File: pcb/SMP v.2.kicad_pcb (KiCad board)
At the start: 2 copper layers, 94.1 x 69.7 mm, 26 parts, among them U1 Elite-C-keebio_without_bottom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

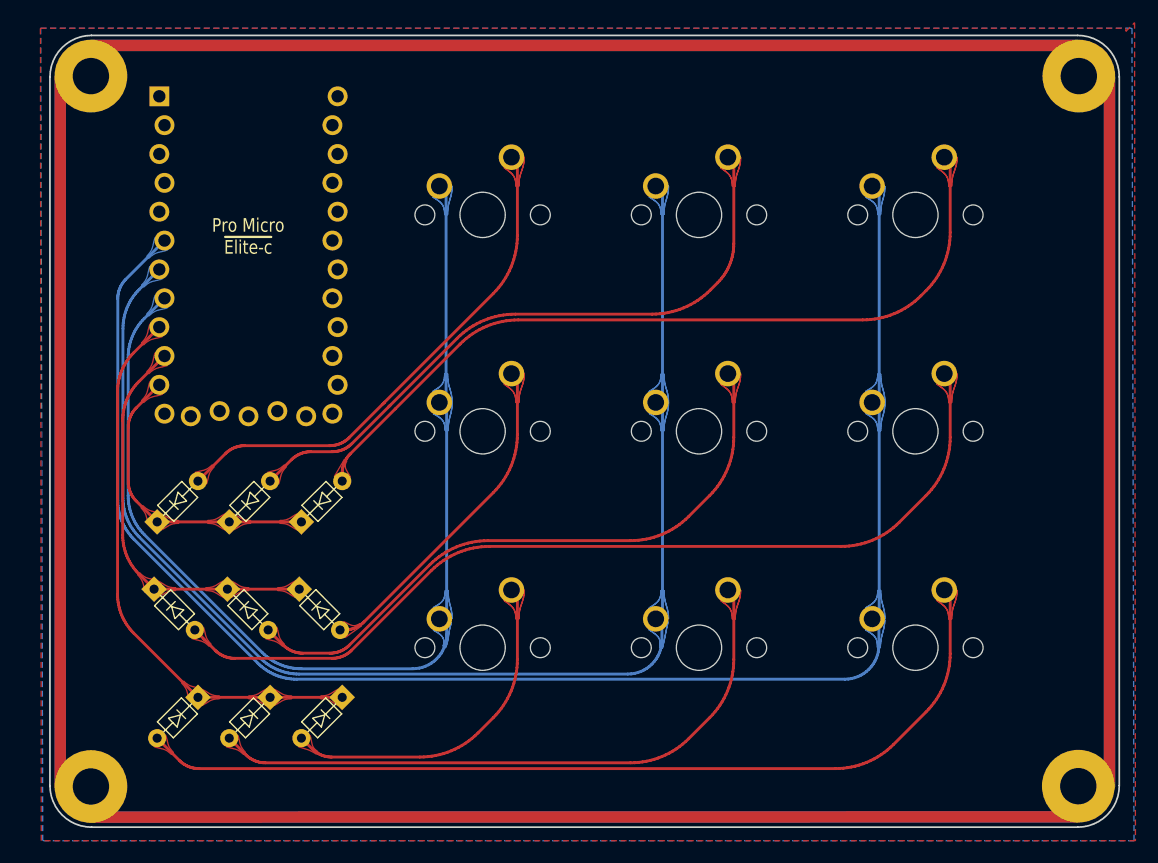
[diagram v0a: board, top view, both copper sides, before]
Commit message: add top plate
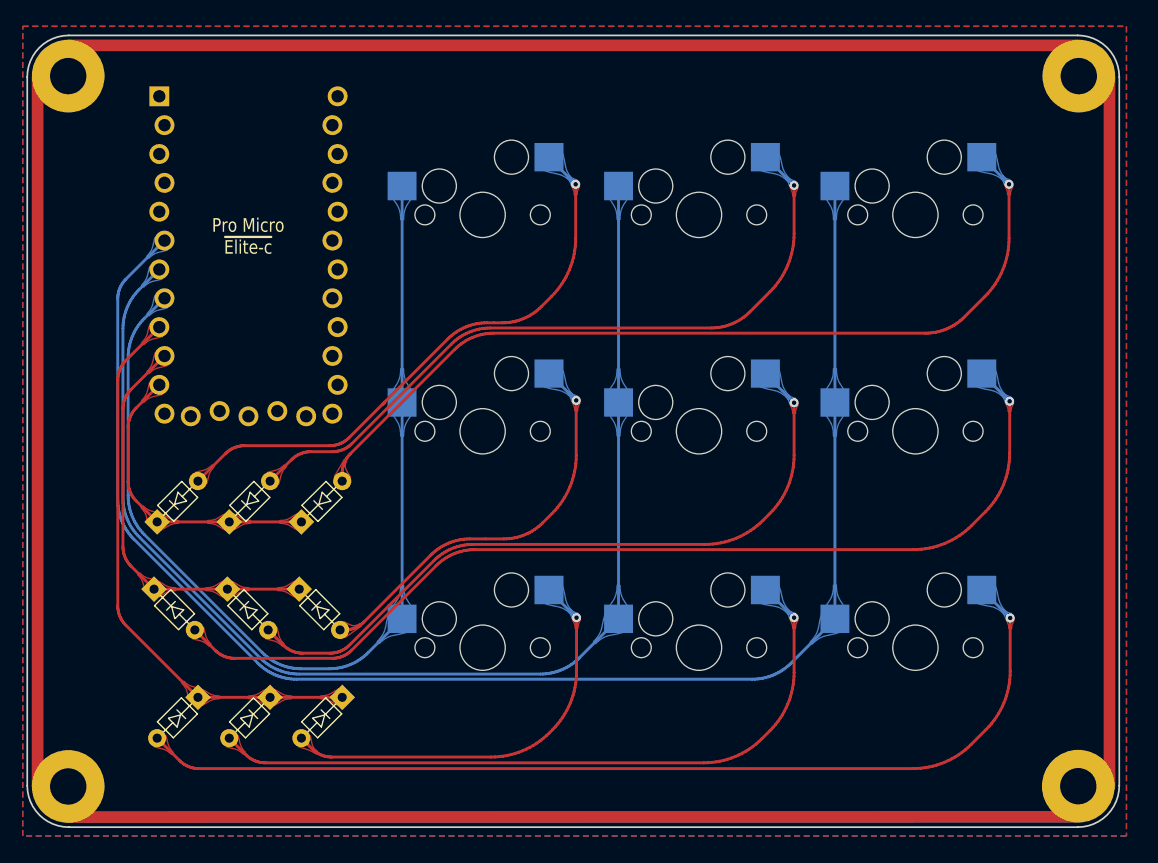
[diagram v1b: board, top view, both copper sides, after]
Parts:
- MX1, MX2, MX3, MX4, MX5, MX6, MX7, MX8, MX9: footprint MX_Only:MXOnly-1U-NoLED -> MX_Only:MXOnly-1U-Hotswap
- moved H1 2.00 mm to (108.8, 66.0)
- moved H3 2.00 mm to (108.8, 128.6)
- renumbered He to H1
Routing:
- net COL0: track 97.5 -> 89.4 mm
- net Net-(D5-Pad2): track 56.1 -> 63.3 mm, vias 0 -> 1
- net COL2: track 142.2 -> 135.0 mm
- net Net-(D9-Pad2): track 82.0 -> 89.0 mm, vias 0 -> 1
- net Net-(D6-Pad2): track 82.0 -> 89.0 mm, vias 0 -> 1
- net Net-(D8-Pad2): track 56.4 -> 63.3 mm, vias 0 -> 1
- net COL1: track 118.7 -> 111.9 mm
- net Net-(D4-Pad2): track 29.7 -> 36.3 mm, vias 0 -> 1
- net Net-(D7-Pad2): track 30.6 -> 37.2 mm, vias 0 -> 1
- net Net-(D2-Pad2): track 57.6 -> 64.1 mm, vias 0 -> 1
- net Net-(D3-Pad2): track 71.1 -> 77.6 mm, vias 0 -> 1
- net Net-(D1-Pad2): track 45.6 -> 51.5 mm, vias 0 -> 1
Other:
- board size 94.1 x 69.7 mm -> 96.1 x 69.7 mm

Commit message: update pcb sch
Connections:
- D1 pad 1: ROW2 -> ROW0
- D2 pad 1: ROW2 -> ROW0
- D3 pad 1: ROW2 -> ROW0
- D7 pad 1: ROW0 -> ROW2
- D8 pad 1: ROW0 -> ROW2
- D9 pad 1: ROW0 -> ROW2
- U1 pad 11: ROW2 -> ROW0
- U1 pad 9: ROW0 -> ROW2
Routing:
- net ROW2: track 26.8 -> 49.5 mm
- net ROW0: track 49.5 -> 26.8 mm
